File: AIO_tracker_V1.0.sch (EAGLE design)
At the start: 66 parts, among them IC1 TPS61201, IC2 TPS61201, J1 EDGE_ICSP, Q1 MOSFET-PCHANNELSMD, U1 ATMEGA328P-AU, U2 USD-SOCKETNEW, X1 SMA-142-0701-881/886, Y2 16MHz

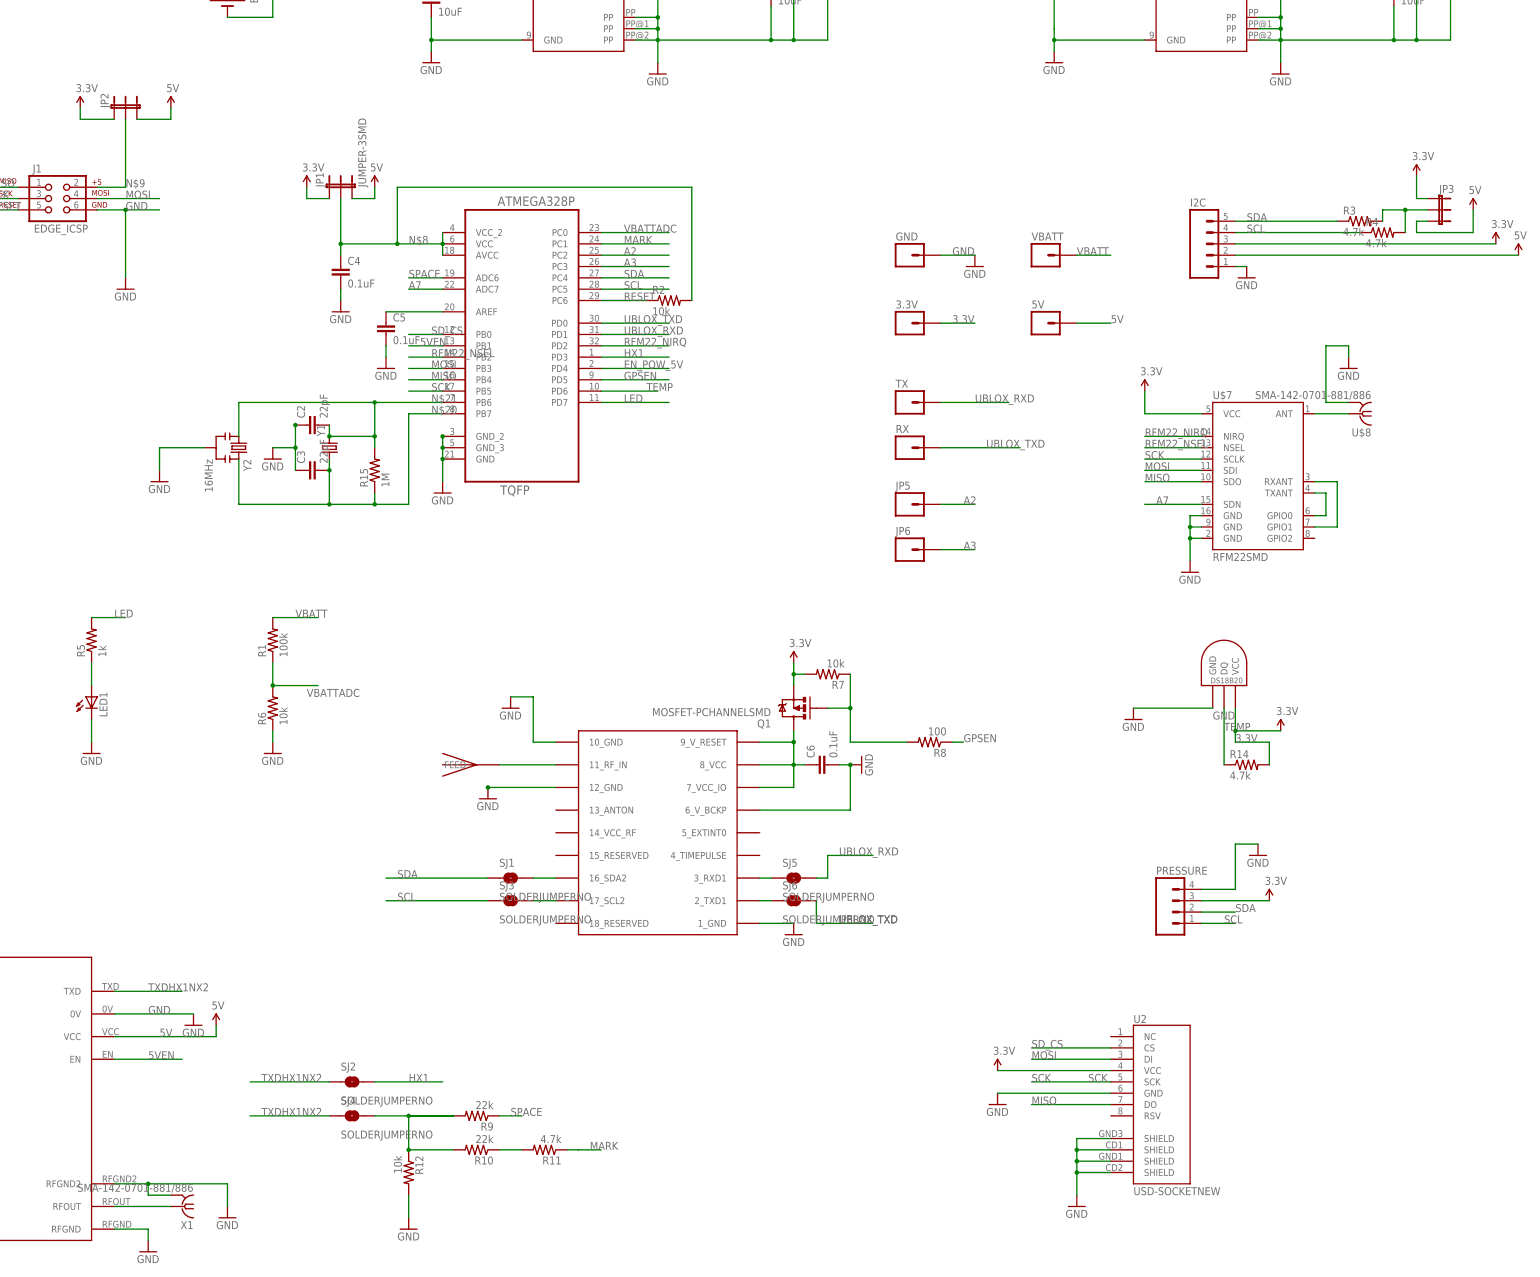
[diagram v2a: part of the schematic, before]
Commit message: removed jumpers and ntx2 support
removed jumpers and ntx2 support
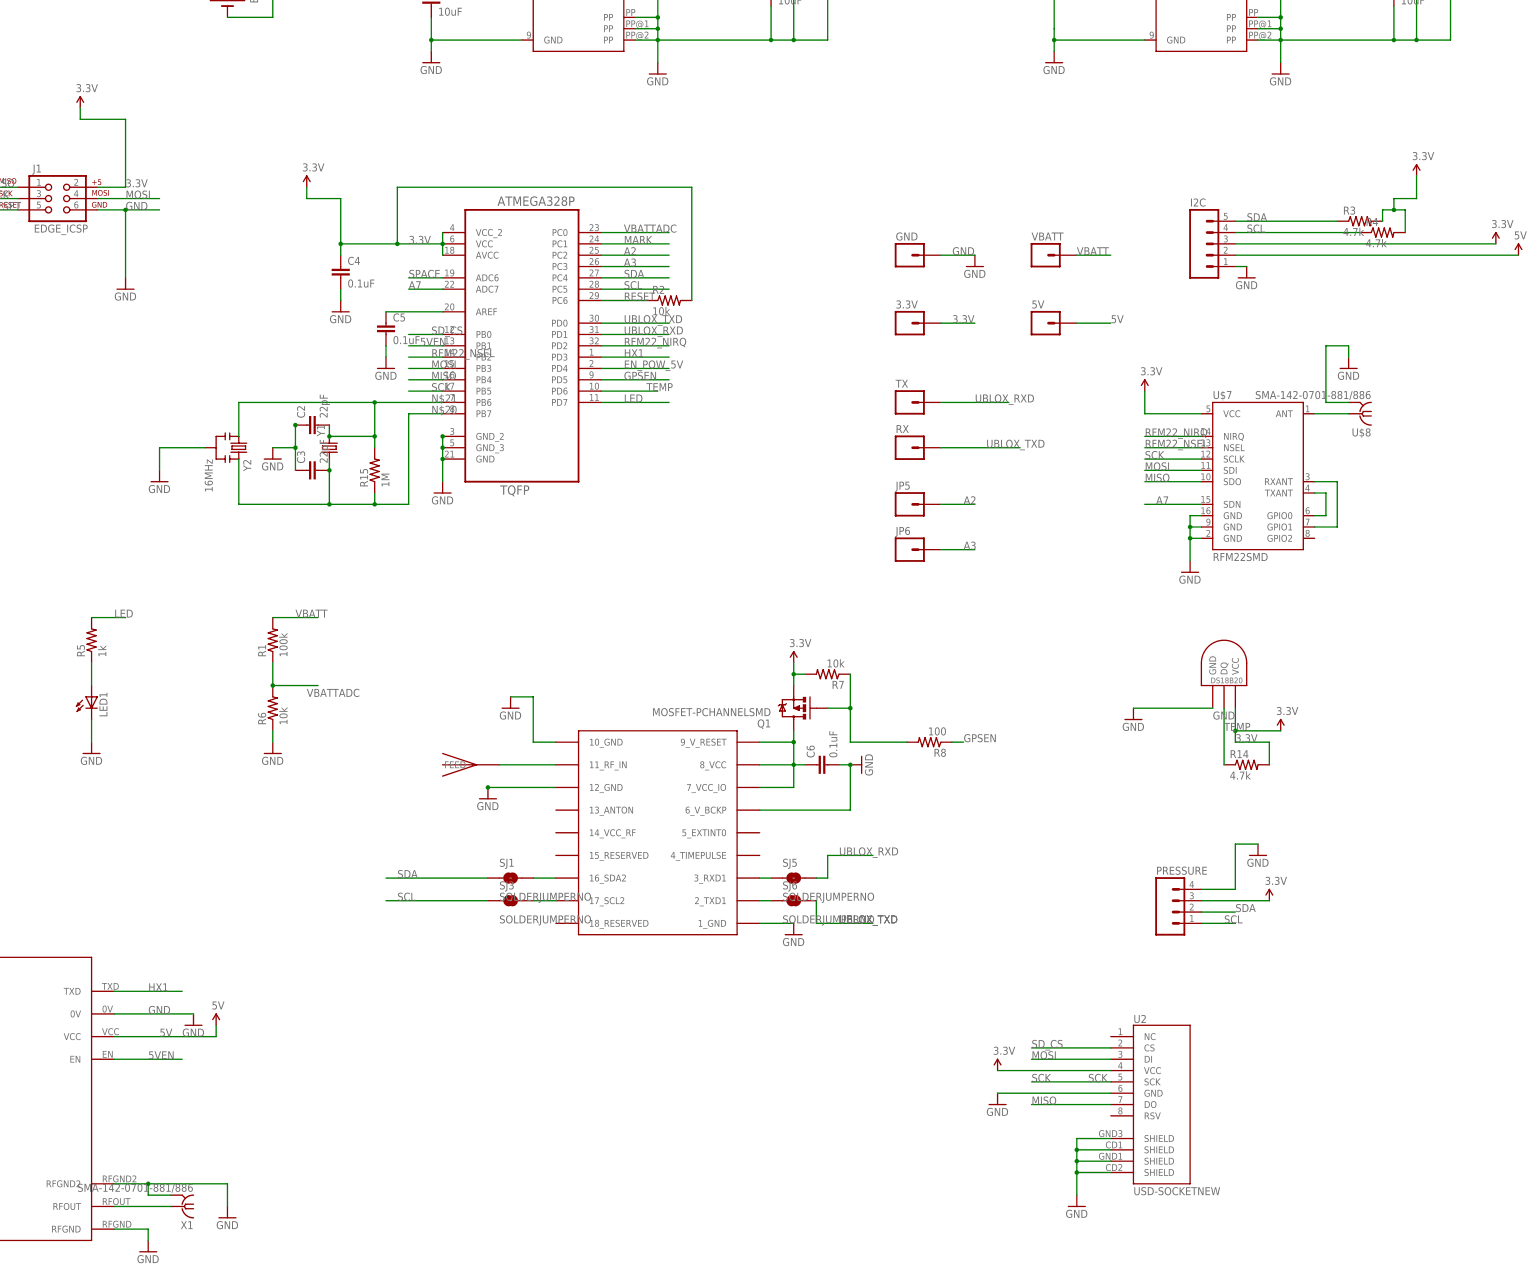
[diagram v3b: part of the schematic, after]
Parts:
- removed JP1, JP2, JP3: JUMPER-3SMD, SparkFun-Passives:JUMPER-3SMD
- removed R10, R9: 22k, SparkFun-Passives:RESISTOR0603-RES
- removed R11: 4.7k, SparkFun-Passives:RESISTOR0603-RES
- removed R12: 10k, SparkFun-Passives:RESISTOR0603-RES
- removed SJ2, SJ4: SOLDERJUMPERNO, SparkFun-Passives:SOLDERJUMPERNO
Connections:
- removed net N$14: JP3.2, R3.2, R4.2
- removed net N$17: R10.2, R12.1, R9.2, SJ4.2
- removed net N$18: R10.1, R11.2
- removed net N$8: C4.1, JP1.2, R2.2, U1.AVCC, U1.VCC, U1.VCC_2
- removed net N$9: J1.2, JP2.2
- removed net TXDHX1NX2: SJ2.1, SJ4.1, U$3.TXD
- net 3.3V: now also C4.1, J1.2, R2.2, R3.2, R4.2, U1.AVCC, U1.VCC, U1.VCC_2; no longer JP1.1, JP2.1, JP3.1
- net 5V: no longer JP1.3, JP2.3, JP3.3
- net GND: no longer R12.2
- net HX1: now also U$3.TXD; no longer SJ2.2
- net MARK: no longer R11.1
- net SPACE: no longer R9.1

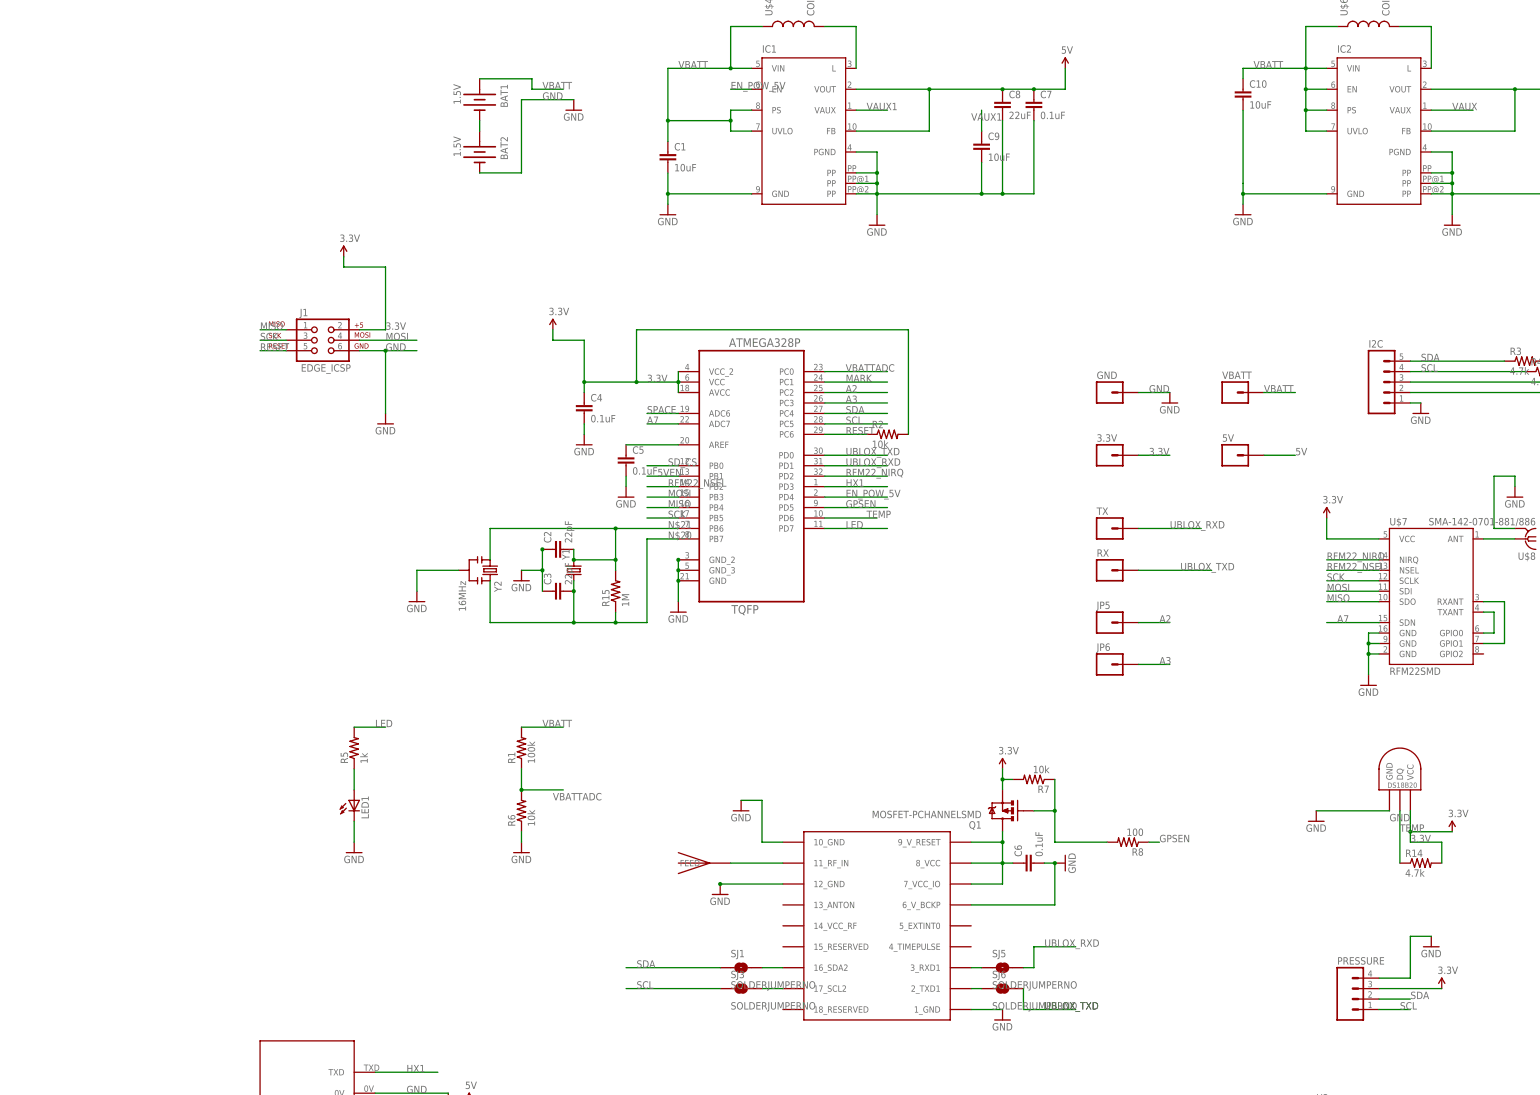
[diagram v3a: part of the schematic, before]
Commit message: added 9dof, new antena, new crystal, cutoff...
added 9dof, new antena, new crystal, cutoff system and changed layout
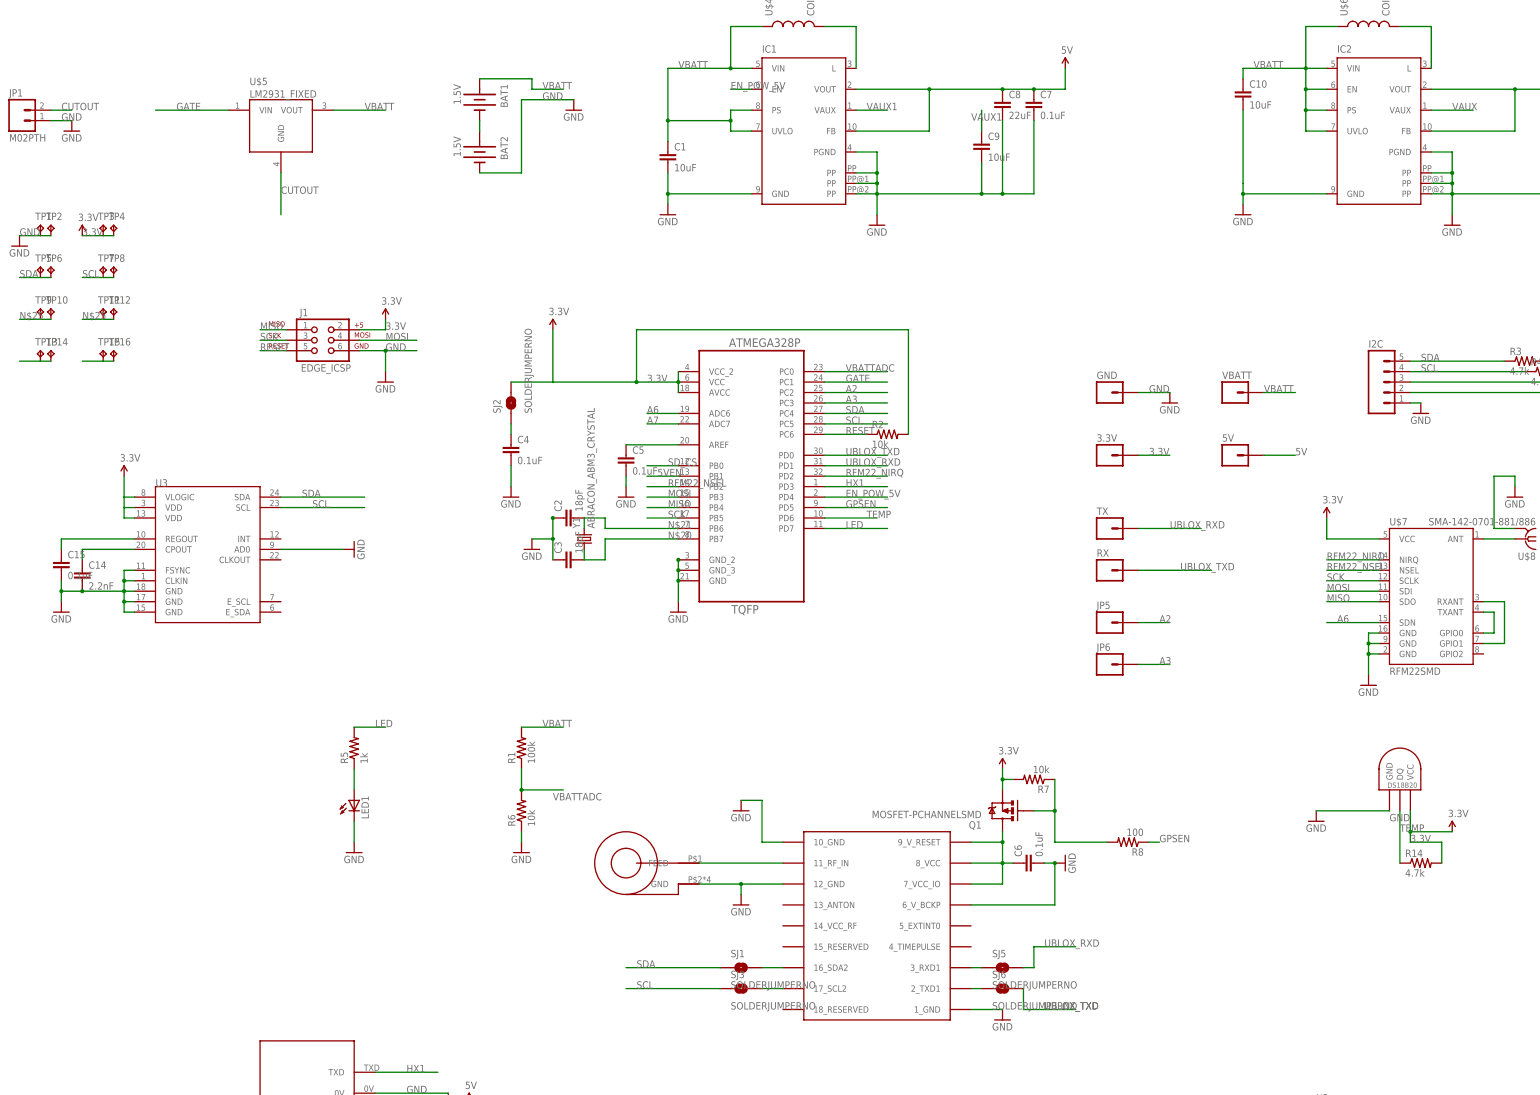
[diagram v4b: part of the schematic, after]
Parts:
- removed PRESSURE: (no value), SparkFun-Connectors:M04PTH
- removed R15: 1M, SparkFun-Passives:RESISTOR0603-RES
- removed Y2: 16MHz, SparkFun-FreqCtrl:RESONATOR16MHZ
- added C14: 2.2nF, SparkFun-Passives:CAP0603-CAP
- added C15: 0.1uF, SparkFun-Passives:CAP0603-CAP
- added JP1: M02PTH, SparkFun-Connectors:M02PTH
- added SJ2: SOLDERJUMPERNO, SparkFun-Passives:SOLDERJUMPERNO
- added TP1, TP10, TP11, TP12, TP13, TP14, TP15, TP16, TP2, TP3, TP4, TP5, TP6, TP7, TP8, TP9: TPTP10SQ, testpad:TPTP10SQ
- added U$5: LM2931_FIXED, SparkFun-PowerIC:LM2931_FIXED
- added U3: (no value), SparkFun-Sensors:MPU-9150QFN-24-NP
- C2, C3: value 22pF -> 18pF
- U$2: value JTI_ANTENNA-1575AT43A40 -> JDGA-REMQV-ANTENNA; device Ava:JTI_ANTENNA-1575AT43A40 -> Ava:JDGA-REMQV-ANTENNA
- Y1: value (none) -> ABRACON_ABM3_CRYSTAL; device SparkFun-FreqCtrl:CRYSTAL10.5X4.8 -> Ava:ABRACON_ABM3_CRYSTAL
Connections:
- removed net MARK: U1.PC1
- removed net SPACE: U1.ADC6
- new net A6: U$7.SDN, U1.ADC6
- new net CUTOUT: JP1.2, U$5.GND
- new net GATE: U$5.VIN, U1.PC1
- new net N$14: TP13.TP, TP14.TP
- new net N$17: C15.1, U3.REGOUT
- new net N$18: C14.1, U3.CPOUT
- new net N$25: TP10.TP, TP11.TP, TP12.TP, TP9.TP
- new net N$8: C4.1, SJ2.1
- new net N$9: TP15.TP, TP16.TP
- net 3.3V: now also SJ2.2, TP3.TP, TP4.TP, U3.VDD@13, U3.VDD@3, U3.VLOGIC; no longer C4.1, PRESSURE.3
- net A7: no longer U$7.SDN
- net GND: now also C14.2, C15.2, JP1.1, TP1.TP, TP2.TP, U$2.GND, U3.AD0, U3.CLKIN, U3.FSYNC, U3.GND@15, U3.GND@17, U3.GND@18; no longer PRESSURE.4, Y2.2
- net N$20: no longer R15.1, Y2.3
- net N$21: no longer R15.2, Y2.1
- net SCL: now also TP7.TP, TP8.TP, U3.SCL; no longer PRESSURE.1
- net SDA: now also TP5.TP, TP6.TP, U3.SDA; no longer PRESSURE.2
- net VBATT: now also U$5.VOUT
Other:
- moved on the sheet: C2, C3, C4, Y1
